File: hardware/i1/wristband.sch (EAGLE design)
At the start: 9 parts, among them M1 MOTOR10MM, Q1 600mA/40V

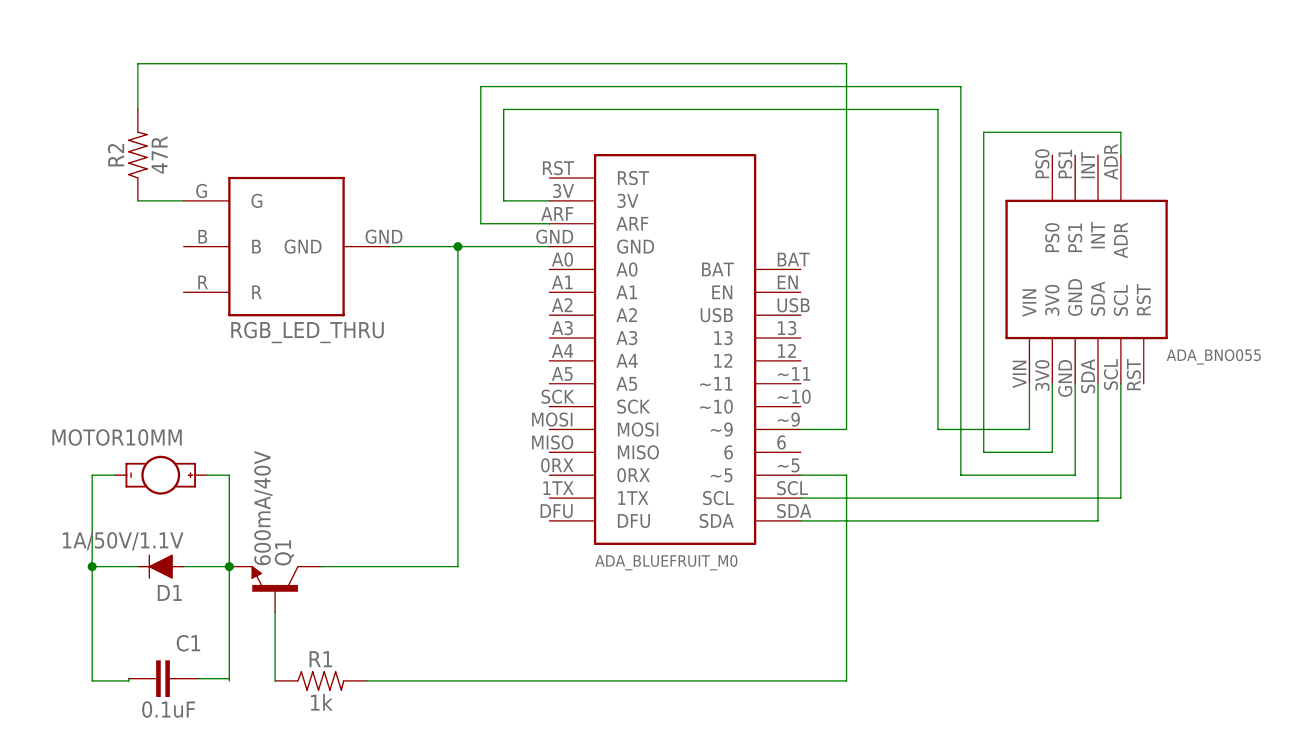
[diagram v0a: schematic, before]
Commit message: Tighten components to allow for mounting holes
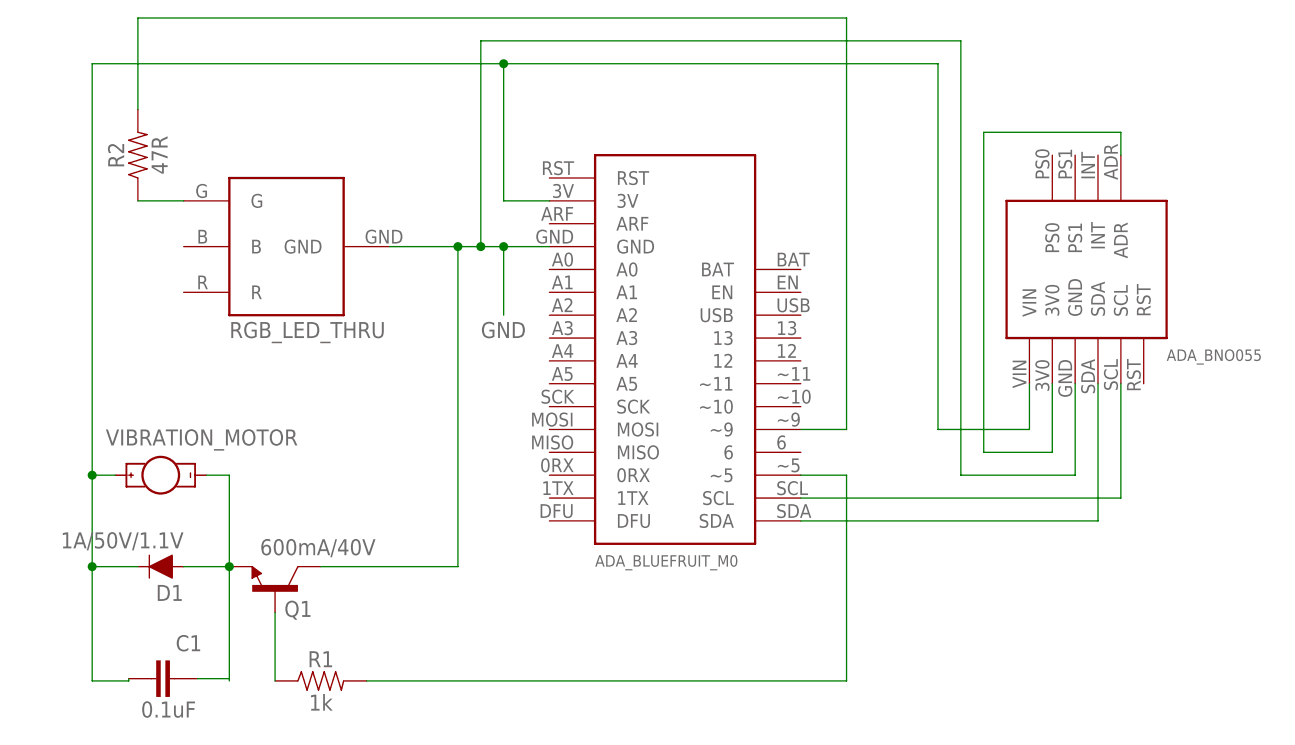
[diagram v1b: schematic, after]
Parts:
- removed M1: MOTOR10MM, SparkFun-Electromechanical:MOTOR10MM
- added U$1: VIBRATION_MOTOR, my_library:VIBRATION_MOTOR
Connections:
- removed net N$12: C1.1, D1.C, M1.-
- removed net N$4: BF1.ARF, BNO1.GND
- removed net N$6: BF1.GND, Q1.C, RGB_LED1.GND
- new net GND: BF1.GND, BNO1.GND, Q1.C, RGB_LED1.GND
- net N$3: now also C1.1, D1.C, U$1.+
- net N$9: now also U$1.-; no longer M1.+
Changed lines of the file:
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@@
 <part name="BF1" library="my_library" deviceset="ADA_BLUEFRUIT_M0" device=""/>
 <part name="BNO1" library="my_library" deviceset="ADA_BNO055" device=""/>
-<part name="M1" library="SparkFun-Electromechanical" library_urn="urn:adsk.eagle:library:516" deviceset="MOTOR" device="10MM" package3d_urn="urn:adsk.eagle:package:38555/1"/>
+<part name="U$1" library="my_library" deviceset="VIBRATION_MOTOR" device=""/>
 </parts>
 <sheets>
@@
 <instances>
 <instance part="Q1" gate="G$1" x="43.18" y="35.56" smashed="yes" rot="MR90">
-<attribute name="NAME" x="43.18" y="38.1" size="1.778" layer="95" font="vector" rot="MR90"/>
-<attribute name="VALUE" x="40.894" y="38.1" size="1.778" layer="96" font="vector" rot="MR90"/>
+<attribute name="NAME" x="44.196" y="34.29" size="1.778" layer="95" font="vector" rot="MR180"/>
+<attribute name="VALUE" x="54.356" y="39.37" size="1.778" layer="96" font="vector" rot="MR0"/>
 </instance>
 <instance part="D1" gate="G$1" x="30.48" y="38.1" smashed="yes" rot="R180">
@@
 <attribute name="VALUE" x="142.24" y="60.96" size="1.27" layer="96"/>
 </instance>
-<instance part="M1" gate="G$1" x="30.48" y="48.26" smashed="yes" rot="R270">
-<attribute name="VALUE" x="33.02" y="53.34" size="1.778" layer="96" font="vector" rot="R180"/>
+<instance part="U$1" gate="G$1" x="30.48" y="48.26" smashed="yes" rot="R90">
+<attribute name="VALUE" x="45.72" y="53.34" size="1.778" layer="96" font="vector" rot="R180"/>
 </instance>
 </instances>
@@
 <pinref part="BF1" gate="G$1" pin="3V"/>
 <wire x1="73.66" y1="78.74" x2="68.58" y2="78.74" width="0.1524" layer="91"/>
-<wire x1="68.58" y1="78.74" x2="68.58" y2="88.9" width="0.1524" layer="91"/>
-<wire x1="68.58" y1="88.9" x2="116.84" y2="88.9" width="0.1524" layer="91"/>
-<wire x1="116.84" y1="88.9" x2="116.84" y2="53.34" width="0.1524" layer="91"/>
+<wire x1="68.58" y1="78.74" x2="68.58" y2="93.98" width="0.1524" layer="91"/>
+<wire x1="68.58" y1="93.98" x2="116.84" y2="93.98" width="0.1524" layer="91"/>
+<wire x1="116.84" y1="93.98" x2="116.84" y2="53.34" width="0.1524" layer="91"/>
 <wire x1="116.84" y1="53.34" x2="127" y2="53.34" width="0.1524" layer="91"/>
 <pinref part="BNO1" gate="G$1" pin="VIN"/>
 <wire x1="127" y1="53.34" x2="127" y2="58.42" width="0.1524" layer="91"/>
-</segment>
-</net>
-<net name="N$4" class="0">
-<segment>
-<pinref part="BF1" gate="G$1" pin="ARF"/>
-<wire x1="73.66" y1="76.2" x2="66.04" y2="76.2" width="0.1524" layer="91"/>
-<wire x1="66.04" y1="76.2" x2="66.04" y2="91.44" width="0.1524" layer="91"/>
-<wire x1="66.04" y1="91.44" x2="119.38" y2="91.44" width="0.1524" layer="91"/>
-<wire x1="119.38" y1="91.44" x2="119.38" y2="48.26" width="0.1524" layer="91"/>
-<wire x1="119.38" y1="48.26" x2="132.08" y2="48.26" width="0.1524" layer="91"/>
-<pinref part="BNO1" gate="G$1" pin="GND"/>
-<wire x1="132.08" y1="48.26" x2="132.08" y2="58.42" width="0.1524" layer="91"/>
+<pinref part="C1" gate="G$1" pin="1"/>
+<wire x1="26.924" y1="25.654" x2="26.924" y2="25.4" width="0.1524" layer="91"/>
+<wire x1="26.924" y1="25.4" x2="22.86" y2="25.4" width="0.1524" layer="91"/>
+<wire x1="22.86" y1="25.4" x2="22.86" y2="38.1" width="0.1524" layer="91"/>
+<pinref part="D1" gate="G$1" pin="C"/>
+<wire x1="22.86" y1="38.1" x2="27.94" y2="38.1" width="0.1524" layer="91"/>
+<junction x="22.86" y="38.1"/>
+<wire x1="68.58" y1="93.98" x2="22.86" y2="93.98" width="0.1524" layer="91"/>
+<wire x1="22.86" y1="93.98" x2="22.86" y2="48.26" width="0.1524" layer="91"/>
+<junction x="68.58" y="93.98"/>
+<wire x1="22.86" y1="48.26" x2="22.86" y2="38.1" width="0.1524" layer="91"/>
+<wire x1="25.4" y1="48.26" x2="22.86" y2="48.26" width="0.1524" layer="91"/>
+<junction x="22.86" y="48.26"/>
+<pinref part="U$1" gate="G$1" pin="+"/>
 </segment>
 </net>
@@
 </segment>
 </net>
-<net name="N$6" class="0">
+<net name="GND" class="0">
 <segment>
 <pinref part="RGB_LED1" gate="G$1" pin="GND"/>
 <pinref part="BF1" gate="G$1" pin="GND"/>
 <wire x1="55.88" y1="73.66" x2="63.5" y2="73.66" width="0.1524" layer="91"/>
-<wire x1="63.5" y1="73.66" x2="73.66" y2="73.66" width="0.1524" layer="91"/>
+<wire x1="63.5" y1="73.66" x2="66.04" y2="73.66" width="0.1524" layer="91"/>
+<wire x1="66.04" y1="73.66" x2="68.58" y2="73.66" width="0.1524" layer="91"/>
+<wire x1="68.58" y1="73.66" x2="73.66" y2="73.66" width="0.1524" layer="91"/>
 <wire x1="63.5" y1="38.1" x2="63.5" y2="73.66" width="0.1524" layer="91"/>
 <junction x="63.5" y="73.66"/>
 <pinref part="Q1" gate="G$1" pin="C"/>
 <wire x1="48.26" y1="38.1" x2="63.5" y2="38.1" width="0.1524" layer="91"/>
+<wire x1="68.58" y1="73.66" x2="68.58" y2="66.04" width="0.1524" layer="91"/>
+<junction x="68.58" y="73.66"/>
+<label x="66.04" y="63.5" size="1.778" layer="95"/>
+<wire x1="66.04" y1="73.66" x2="66.04" y2="96.52" width="0.1524" layer="91"/>
+<wire x1="66.04" y1="96.52" x2="119.38" y2="96.52" width="0.1524" layer="91"/>
+<wire x1="119.38" y1="96.52" x2="119.38" y2="48.26" width="0.1524" layer="91"/>
+<wire x1="119.38" y1="48.26" x2="132.08" y2="48.26" width="0.1524" layer="91"/>
+<pinref part="BNO1" gate="G$1" pin="GND"/>
+<wire x1="132.08" y1="48.26" x2="132.08" y2="58.42" width="0.1524" layer="91"/>
+<junction x="66.04" y="73.66"/>
 </segment>
 </net>
@@
 <segment>
 <pinref part="R2" gate="G$1" pin="2"/>
-<wire x1="27.94" y1="88.9" x2="27.94" y2="93.98" width="0.1524" layer="91"/>
-<wire x1="27.94" y1="93.98" x2="106.68" y2="93.98" width="0.1524" layer="91"/>
-<wire x1="106.68" y1="93.98" x2="106.68" y2="53.34" width="0.1524" layer="91"/>
+<wire x1="27.94" y1="88.9" x2="27.94" y2="99.06" width="0.1524" layer="91"/>
+<wire x1="27.94" y1="99.06" x2="106.68" y2="99.06" width="0.1524" layer="91"/>
+<wire x1="106.68" y1="99.06" x2="106.68" y2="53.34" width="0.1524" layer="91"/>
 <pinref part="BF1" gate="G$1" pin="~9"/>
 <wire x1="106.68" y1="53.34" x2="101.6" y2="53.34" width="0.1524" layer="91"/>
@@
 <wire x1="38.1" y1="25.654" x2="38.1" y2="38.1" width="0.1524" layer="91"/>
 <junction x="38.1" y="38.1"/>
-<pinref part="M1" gate="G$1" pin="+"/>
+<wire x1="38.1" y1="48.26" x2="38.1" y2="38.1" width="0.1524" layer="91"/>
 <wire x1="35.56" y1="48.26" x2="38.1" y2="48.26" width="0.1524" layer="91"/>
-<wire x1="38.1" y1="48.26" x2="38.1" y2="38.1" width="0.1524" layer="91"/>
+<pinref part="U$1" gate="G$1" pin="-"/>
 </segment>
 </net>
@@
 </segment>
 </net>
-<net name="N$12" class="0">
-<segment>
-<pinref part="C1" gate="G$1" pin="1"/>
-<wire x1="26.924" y1="25.654" x2="26.924" y2="25.4" width="0.1524" layer="91"/>
-<wire x1="26.924" y1="25.4" x2="22.86" y2="25.4" width="0.1524" layer="91"/>
-<wire x1="22.86" y1="25.4" x2="22.86" y2="38.1" width="0.1524" layer="91"/>
-<pinref part="D1" gate="G$1" pin="C"/>
-<wire x1="22.86" y1="38.1" x2="27.94" y2="38.1" width="0.1524" layer="91"/>
-<pinref part="M1" gate="G$1" pin="-"/>
-<wire x1="25.4" y1="48.26" x2="22.86" y2="48.26" width="0.1524" layer="91"/>
-<wire x1="22.86" y1="48.26" x2="22.86" y2="38.1" width="0.1524" layer="91"/>
-<junction x="22.86" y="38.1"/>
-</segment>
-</net>
